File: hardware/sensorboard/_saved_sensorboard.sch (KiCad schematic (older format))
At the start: 15 parts, among them P1 PWR, P2 PROG, U1 ESP-07v2, U2 TC1262, U3 BMP180_board, U4 DHT22

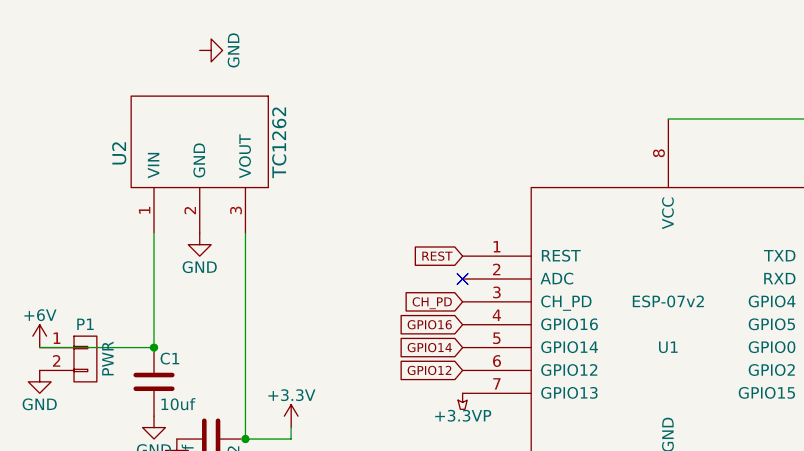
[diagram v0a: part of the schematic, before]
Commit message: Measure the actual battery voltage on ADC pin.
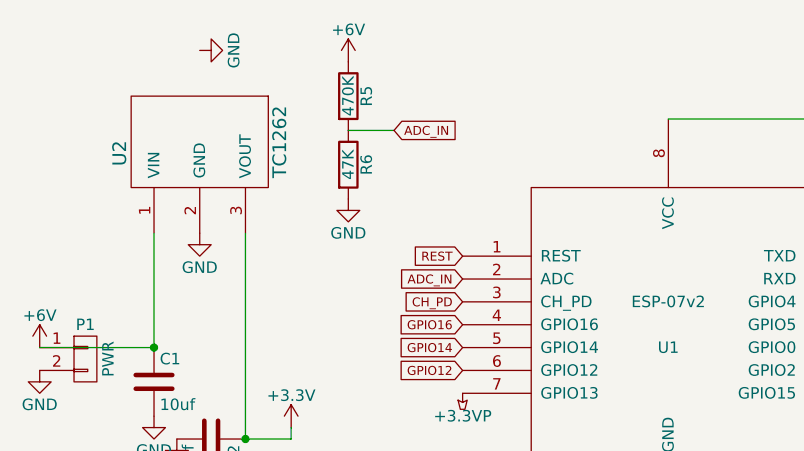
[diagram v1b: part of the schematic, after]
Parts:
- added R5: 470K, Resistors_SMD:R_0603_HandSoldering, symbol R
- added R6: 47K, Resistors_SMD:R_0603_HandSoldering, symbol R
- C3, C4, C5: footprint Capacitors_SMD:C_0805_HandSoldering -> Capacitors_SMD:C_0603_HandSoldering
- R1, R2, R3, R4: footprint Resistors_SMD:R_1206_HandSoldering -> Resistors_SMD:R_0603_HandSoldering
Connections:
- net +6V: now also R5.1
- net GND: now also R6.2
- net ADC_IN: now reaches U1.2 (ADC)
- net ADC_IN: now also R5.2, R6.1
- no-connect marks 3 -> 2
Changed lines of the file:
@@
 F 0 "C3" H 4525 1150 50  0000 L CNN
 F 1 "100nf" H 4525 950 50  0000 L CNN
-F 2 "Capacitors_SMD:C_0805_HandSoldering" H 4538 900 30  0001 C CNN
+F 2 "Capacitors_SMD:C_0603_HandSoldering" H 4538 900 30  0001 C CNN
 F 3 "" H 4500 1050 60  0000 C CNN
 	1    4500 1050
@@
 Text GLabel 2450 1500 0    39   Input ~ 0
 REST
-NoConn ~ 2450 1600
 $Comp
 L BMP180_board U3
@@
 F 0 "C4" H 925 3700 50  0000 L CNN
 F 1 "100nf" H 925 3500 50  0000 L CNN
-F 2 "Capacitors_SMD:C_0805_HandSoldering" H 938 3450 30  0001 C CNN
+F 2 "Capacitors_SMD:C_0603_HandSoldering" H 938 3450 30  0001 C CNN
 F 3 "" H 900 3600 60  0000 C CNN
 	1    900  3600
@@
 F 0 "C5" H 2025 3750 50  0000 L CNN
 F 1 "100nf" H 2025 3550 50  0000 L CNN
-F 2 "Capacitors_SMD:C_0805_HandSoldering" H 2038 3500 30  0001 C CNN
+F 2 "Capacitors_SMD:C_0603_HandSoldering" H 2038 3500 30  0001 C CNN
 F 3 "" H 2000 3650 60  0000 C CNN
 	1    2000 3650
@@
 F 0 "R1" V 3130 3350 50  0000 C CNN
 F 1 "10k" V 3050 3350 50  0000 C CNN
-F 2 "Resistors_SMD:R_1206_HandSoldering" V 2980 3350 30  0001 C CNN
+F 2 "Resistors_SMD:R_0603_HandSoldering" V 2980 3350 30  0001 C CNN
 F 3 "" H 3050 3350 30  0000 C CNN
 	1    3050 3350
@@
 F 0 "R2" V 3380 3500 50  0000 C CNN
 F 1 "10k" V 3300 3500 50  0000 C CNN
-F 2 "Resistors_SMD:R_1206_HandSoldering" V 3230 3500 30  0001 C CNN
+F 2 "Resistors_SMD:R_0603_HandSoldering" V 3230 3500 30  0001 C CNN
 F 3 "" H 3300 3500 30  0000 C CNN
 	1    3300 3500
@@
 F 0 "R3" V 5330 3050 50  0000 C CNN
 F 1 "10k" V 5250 3050 50  0000 C CNN
-F 2 "Resistors_SMD:R_1206_HandSoldering" V 5180 3050 30  0001 C CNN
+F 2 "Resistors_SMD:R_0603_HandSoldering" V 5180 3050 30  0001 C CNN
 F 3 "" H 5250 3050 30  0000 C CNN
 	1    5250 3050
@@
 F 0 "R4" V 5780 3050 50  0000 C CNN
 F 1 "10k" V 5700 3050 50  0000 C CNN
-F 2 "Resistors_SMD:R_1206_HandSoldering" V 5630 3050 30  0001 C CNN
+F 2 "Resistors_SMD:R_0603_HandSoldering" V 5630 3050 30  0001 C CNN
 F 3 "" H 5700 3050 30  0000 C CNN
 	1    5700 3050
@@
 	0    -1   -1   0
 $EndComp
+Text GLabel 2450 1600 0    39   Input ~ 0
+ADC_IN
+Text GLabel 2150 950  2    39   Input ~ 0
+ADC_IN
+$Comp
+L GND #PWR022
+U 1 1 562D40D4
+P 1950 1250
+F 0 "#PWR022" H 1950 1000 50  0001 C CNN
+F 1 "GND" H 1950 1100 50  0000 C CNN
+F 2 "" H 1950 1250 60  0000 C CNN
+F 3 "" H 1950 1250 60  0000 C CNN
+	1    1950 1250
+	1    0    0    -1
+$EndComp
+$Comp
+L +6V #PWR023
+U 1 1 562D410C
+P 1950 650
+F 0 "#PWR023" H 1950 500 50  0001 C CNN
+F 1 "+6V" H 1950 790 50  0000 C CNN
+F 2 "" H 1950 650 60  0000 C CNN
+F 3 "" H 1950 650 60  0000 C CNN
+	1    1950 650
+	1    0    0    -1
+$EndComp
+$Comp
+L R R5
+U 1 1 562D41A2
+P 1950 800
+F 0 "R5" V 2030 800 50  0000 C CNN
+F 1 "470K" V 1950 800 50  0000 C CNN
+F 2 "Resistors_SMD:R_0603_HandSoldering" V 1880 800 30  0001 C CNN
+F 3 "" H 1950 800 30  0000 C CNN
+	1    1950 800
+	1    0    0    -1
+$EndComp
+$Comp
+L R R6
+U 1 1 562D41F0
+P 1950 1100
+F 0 "R6" V 2030 1100 50  0000 C CNN
+F 1 "47K" V 1950 1100 50  0000 C CNN
+F 2 "Resistors_SMD:R_0603_HandSoldering" V 1880 1100 30  0001 C CNN
+F 3 "" H 1950 1100 30  0000 C CNN
+	1    1950 1100
+	1    0    0    -1
+$EndComp
+Wire Wire Line
+	1950 950  2150 950
 $EndSCHEMATC
